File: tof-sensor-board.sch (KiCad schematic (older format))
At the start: 28 parts, among them U1 STM32F302K8U6, U2 LTC2875, U3 MCP1703, U4 VL53L0X, X1 16MHz

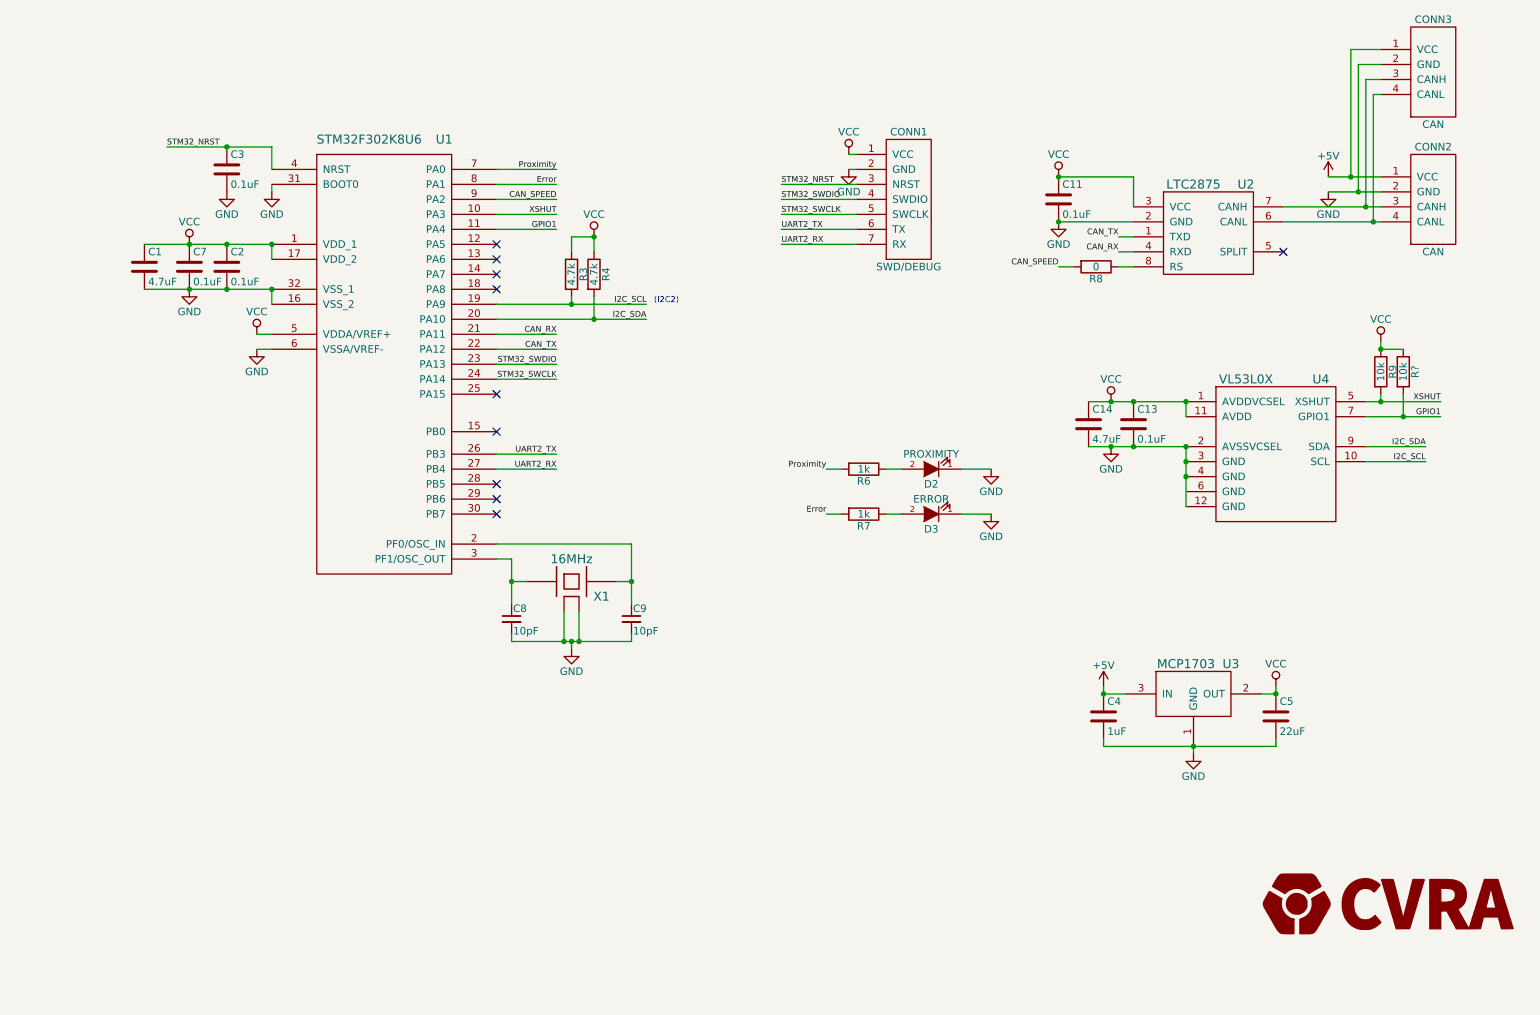
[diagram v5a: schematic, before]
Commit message: Start placing footprints
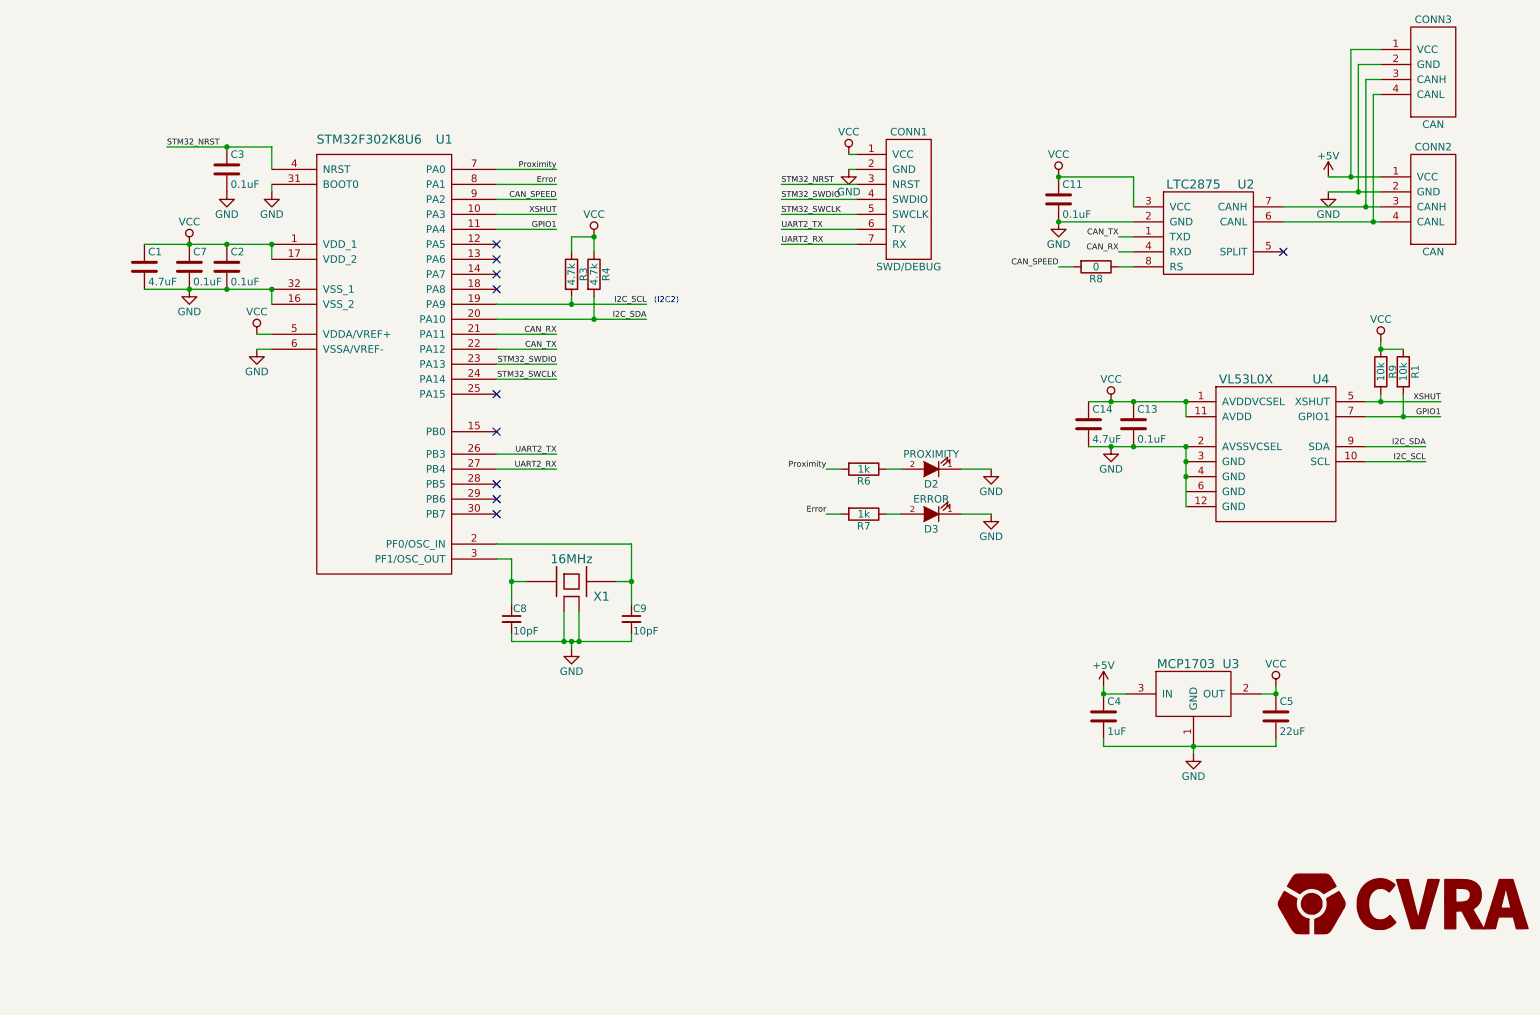
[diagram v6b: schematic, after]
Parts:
- C13: footprint (none) -> Capacitors_SMD:C_0402
- C14: footprint Capacitors_SMD:C_0402 -> Capacitors_SMD:C_0603
- C4, C5: footprint (none) -> Capacitors_SMD:C_0603
- CONN1: footprint Connectors_Molex:Connector_Molex_PicoBlade_53048-0710 -> Connectors_Molex:Connector_Molex_PicoBlade_53047-0710
- D2, D3: footprint _std:_0603 -> LEDs:LED-0603
- U4: footprint (none) -> _sensors:VL53L0X
- gave numbers to parts that had none: 1

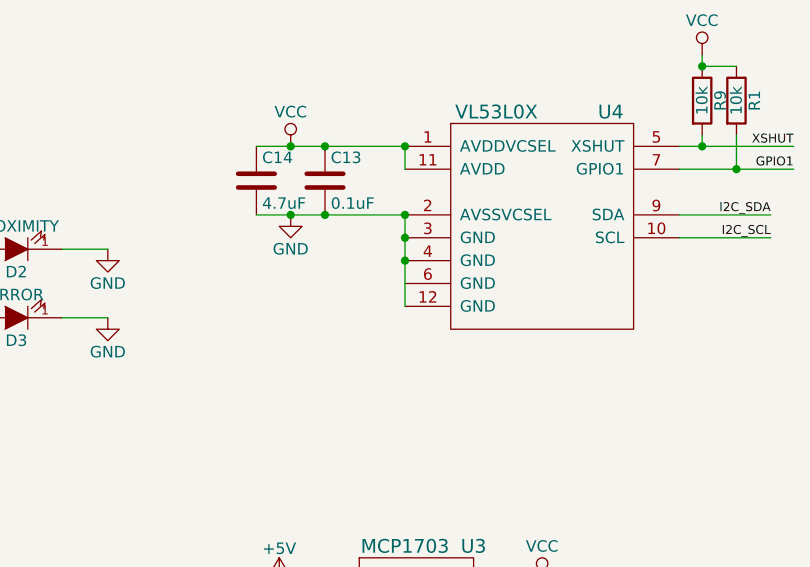
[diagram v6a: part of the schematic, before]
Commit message: LDO footprint, fix unconnected GND pin
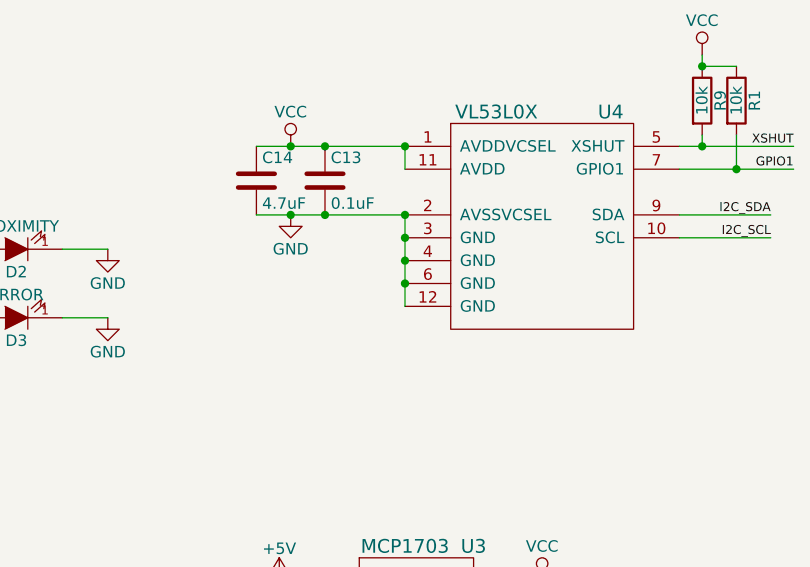
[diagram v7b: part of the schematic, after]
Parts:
- U3: footprint (none) -> _std:SOT-23
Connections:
- net GND: now also U4.6 (GND)
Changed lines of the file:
@@
 F 0 "U3" H 9100 5600 60  0000 C CNN
 F 1 "MCP1703" H 8800 5600 60  0000 C CNN
-F 2 "" H 8750 5850 60  0001 C CNN
+F 2 "_std:SOT-23" H 8750 5850 60  0001 C CNN
 F 3 "" H 8750 5850 60  0000 C CNN
 	1    8850 5400
@@
 Connection ~ 2700 2400
 Connection ~ 2700 2700
+Connection ~ 8800 4050
 $EndSCHEMATC

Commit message: routing
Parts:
- added MEC1, MEC2: MEC, _mech:_M2, symbol MEC
- R8: value 0 -> 1k
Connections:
- net CAN_SPEED: now also U1.15 (PB0); no longer U1.9 (PA2)
- net Error: now also U1.12 (PA5); no longer U1.8 (PA1)
- net GPIO1: now also U1.13 (PA6); no longer U1.11 (PA4)
- net Proximity: now also U1.11 (PA4); no longer U1.7 (PA0)
- net XSHUT: now also U1.9 (PA2); no longer U1.10 (PA3)
- no-connect marks 10 -> 12
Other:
- moved on the sheet: R3, R4
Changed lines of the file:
@@
 Text Label 6400 4200 2    39   ~ 0
 Error
-Text Label 4600 2000 2    39   ~ 0
+Text Label 4600 2400 2    39   ~ 0
 Error
-Text Label 4600 1900 2    39   ~ 0
+Text Label 4600 2300 2    39   ~ 0
 Proximity
-Text Label 5200 2800 2    39   ~ 0
+Text Label 5500 2800 2    39   ~ 0
 I2C_SCL
-Text Label 5200 2900 2    39   ~ 0
+Text Label 5500 2900 2    39   ~ 0
 I2C_SDA
 $Comp
 L R R3
 U 1 1 5580B966
-P 4700 2600
-F 0 "R3" V 4780 2600 50  0000 C CNN
-F 1 "4.7k" V 4700 2600 50  0000 C CNN
-F 2 "Resistors_SMD:R_0402" V 4630 2600 30  0001 C CNN
-F 3 "" H 4700 2600 30  0000 C CNN
-	1    4700 2600
+P 5000 2600
+F 0 "R3" V 5080 2600 50  0000 C CNN
+F 1 "4.7k" V 5000 2600 50  0000 C CNN
+F 2 "Resistors_SMD:R_0402" V 4930 2600 30  0001 C CNN
+F 3 "" H 5000 2600 30  0000 C CNN
+	1    5000 2600
 	1    0    0    -1
 $EndComp
@@
 L R R4
 U 1 1 5580BA95
-P 4850 2600
-F 0 "R4" V 4930 2600 50  0000 C CNN
-F 1 "4.7k" V 4850 2600 50  0000 C CNN
-F 2 "Resistors_SMD:R_0402" V 4780 2600 30  0001 C CNN
-F 3 "" H 4850 2600 30  0000 C CNN
-	1    4850 2600
+P 5150 2600
+F 0 "R4" V 5230 2600 50  0000 C CNN
+F 1 "4.7k" V 5150 2600 50  0000 C CNN
+F 2 "Resistors_SMD:R_0402" V 5080 2600 30  0001 C CNN
+F 3 "" H 5150 2600 30  0000 C CNN
+	1    5150 2600
 	1    0    0    -1
 $EndComp
@@
 	1    0    0    -1
 $EndComp
-Text Label 4600 2300 2    39   ~ 0
+Text Label 4600 2500 2    39   ~ 0
 GPIO1
 $Comp
@@
 P 8200 2550
 F 0 "R8" V 8280 2550 50  0000 C CNN
-F 1 "0" V 8200 2550 50  0000 C CNN
+F 1 "1k" V 8200 2550 50  0000 C CNN
 F 2 "Resistors_SMD:R_0402" V 8130 2550 30  0001 C CNN
 F 3 "" H 8200 2550 30  0000 C CNN
@@
 Text Label 7950 2550 2    39   ~ 0
 CAN_SPEED
-Text Label 4600 2100 2    39   ~ 0
+Text Label 4600 3650 2    39   ~ 0
 CAN_SPEED
 $Comp
@@
 	1    0    0    -1
 $EndComp
-NoConn ~ 4200 2400
-NoConn ~ 4200 2500
-NoConn ~ 4200 2600
 NoConn ~ 4200 2700
 NoConn ~ 4200 3400
@@
 	1    0    0    -1
 $EndComp
-NoConn ~ 4200 3650
 $Comp
 L C C3
@@
 L VCC #PWR017
 U 1 1 574E1BFC
-P 4850 2350
-F 0 "#PWR017" H 4850 2200 50  0001 C CNN
-F 1 "VCC" H 4850 2500 50  0000 C CNN
-F 2 "" H 4850 2350 50  0000 C CNN
-F 3 "" H 4850 2350 50  0000 C CNN
-	1    4850 2350
+P 5150 2350
+F 0 "#PWR017" H 5150 2200 50  0001 C CNN
+F 1 "VCC" H 5150 2500 50  0000 C CNN
+F 2 "" H 5150 2350 50  0000 C CNN
+F 3 "" H 5150 2350 50  0000 C CNN
+	1    5150 2350
 	1    0    0    -1
 $EndComp
@@
 	6400 4200 6500 4200
 Wire Wire Line
-	4600 1900 4200 1900
-Wire Wire Line
-	4200 2000 4600 2000
+	4600 2300 4200 2300
+Wire Wire Line
+	4200 2400 4600 2400
 Wire Wire Line
 	4600 3200 4200 3200
@@
 	4200 3300 4600 3300
 Wire Wire Line
-	4200 2900 5200 2900
-Wire Wire Line
-	4200 2800 5200 2800
-Wire Wire Line
-	4700 2350 4850 2350
-Wire Wire Line
-	4850 2350 4850 2450
-Wire Wire Line
-	4700 2350 4700 2450
-Connection ~ 4850 2350
-Wire Wire Line
-	4700 2800 4700 2750
-Wire Wire Line
-	4850 2900 4850 2750
-Connection ~ 4700 2800
-Connection ~ 4850 2900
+	4200 2900 5500 2900
+Wire Wire Line
+	4200 2800 5500 2800
+Wire Wire Line
+	5000 2350 5150 2350
+Wire Wire Line
+	5150 2350 5150 2450
+Wire Wire Line
+	5000 2350 5000 2450
+Connection ~ 5150 2350
+Wire Wire Line
+	5000 2800 5000 2750
+Wire Wire Line
+	5150 2900 5150 2750
+Connection ~ 5000 2800
+Connection ~ 5150 2900
 Wire Wire Line
 	10000 3450 10500 3450
@@
 Connection ~ 10100 3450
 Wire Wire Line
-	4600 2200 4200 2200
-Wire Wire Line
-	4200 2300 4600 2300
+	4600 2100 4200 2100
+Wire Wire Line
+	4200 2500 4600 2500
 Wire Wire Line
 	8350 2450 8450 2450
@@
 	2700 2700 2700 2800
 Wire Wire Line
-	4200 2100 4600 2100
+	4200 3650 4600 3650
 Wire Wire Line
 	4200 3800 4600 3800
@@
 Connection ~ 8800 3850
 Connection ~ 8800 3750
-Text Label 4600 2200 2    39   ~ 0
+Text Label 4600 2100 2    39   ~ 0
 XSHUT
 $Comp
@@
 Wire Wire Line
 	6600 2400 6100 2400
-Text Notes 5250 2800 0    40   ~ 0
+Text Notes 5550 2800 0    40   ~ 0
 (I2C2)
 Connection ~ 2400 1750
@@
 Connection ~ 2700 2700
 Connection ~ 8800 4050
+NoConn ~ 4200 1900
+NoConn ~ 4200 2000
+$Comp
+L MEC MEC2
+U 1 1 57C3F6D7
+P 1600 7200
+F 0 "MEC2" H 1600 7000 60  0000 C CNN
+F 1 "MEC" H 1600 7350 60  0000 C CNN
+F 2 "_mech:_M2" H 1600 7200 60  0001 C CNN
+F 3 "" H 1600 7200 60  0000 C CNN
+	1    1600 7200
+	1    0    0    -1
+$EndComp
+$Comp
+L MEC MEC1
+U 1 1 57C3F8BD
+P 1150 7200
+F 0 "MEC1" H 1150 7000 60  0000 C CNN
+F 1 "MEC" H 1150 7350 60  0000 C CNN
+F 2 "_mech:_M2" H 1150 7200 60  0001 C CNN
+F 3 "" H 1150 7200 60  0000 C CNN
+	1    1150 7200
+	1    0    0    -1
+$EndComp
+NoConn ~ 1450 7200
+NoConn ~ 1000 7200
+NoConn ~ 4200 2200
+NoConn ~ 4200 2600
 $EndSCHEMATC
